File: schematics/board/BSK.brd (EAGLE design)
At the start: 94 x 94 mm, 58 parts

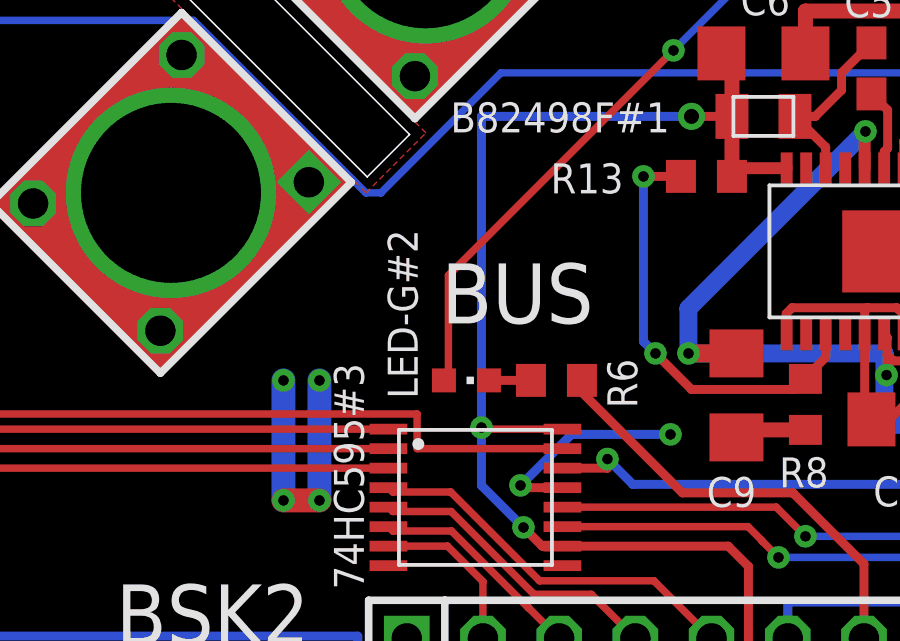
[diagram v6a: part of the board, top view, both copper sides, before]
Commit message: Исправлены RADIO и диоды
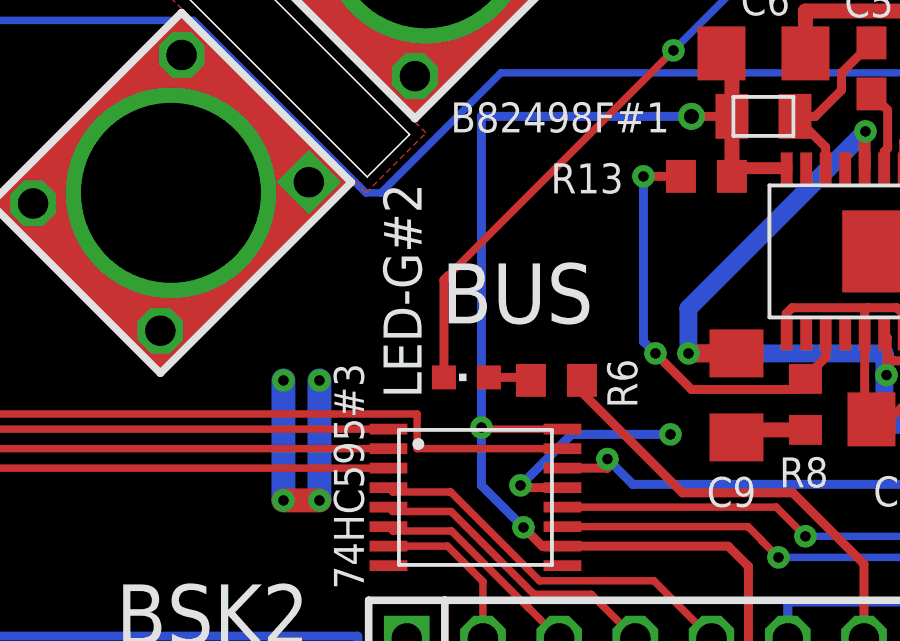
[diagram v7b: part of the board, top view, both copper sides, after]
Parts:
- moved LED-G#2 0.10 mm to (32.1, 16.1), turned to 90 degrees
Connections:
- net BUS-: now also LED-G#2.C; no longer LED-G#2.A
- net N$38: now also LED-G#2.A; no longer LED-G#2.C
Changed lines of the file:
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@@
 <attribute name="VALUE" x="18.405" y="56.53" size="1.27" layer="27" rot="R90"/>
-</element>
-<element name="LED-G#2" library="led" library_urn="urn:adsk.eagle:library:259" package="CHIPLED_0603" package3d_urn="urn:adsk.eagle:package:15822/2" value="" x="32.1" y="16" smashed="yes" rot="R270">
-<attribute name="NAME" x="30.475" y="15.39" size="1" layer="25" rot="R90"/>
-<attribute name="POPULARITY" value="28" x="30.1" y="37" size="1.778" layer="27" rot="R270" display="off"/>
-<attribute name="VALUE" x="30.83" y="14.095" size="1.27" layer="27"/>
 </element>
 <element name="R6" library="resistor" library_urn="urn:adsk.eagle:library:348" package="R0603" package3d_urn="urn:adsk.eagle:package:23555/3" value="2k" x="35.1" y="16" smashed="yes" rot="R180">
@@
 <element name="R14" library="resistor" library_urn="urn:adsk.eagle:library:348" package="R0603" package3d_urn="urn:adsk.eagle:package:23555/3" value="5k1" x="62.1" y="78.7" smashed="yes" rot="R180">
 <attribute name="VALUE" x="62.735" y="80.605" size="1.27" layer="27" rot="R180"/>
+</element>
+<element name="LED-G#2" library="led" library_urn="urn:adsk.eagle:library:259" package="CHIPLED_0603" package3d_urn="urn:adsk.eagle:package:15822/2" value="" x="32.1" y="16.1" smashed="yes" rot="R90">
+<attribute name="NAME" x="29.335" y="22.57" size="1.27" layer="25" rot="R270"/>
+<attribute name="POPULARITY" value="28" x="23.5" y="11.1" size="1.778" layer="27" rot="R90" display="off"/>
+<attribute name="VALUE" x="33.37" y="18.005" size="1.27" layer="27" rot="R180"/>
 </element>
 </elements>
@@
 <contactref element="R20" pad="2"/>
 <contactref element="FS8205A" pad="23"/>
-<contactref element="LED-G#2" pad="A"/>
 <contactref element="U$4" pad="3"/>
 <contactref element="U$4" pad="4"/>
@@
 <wire x1="67.5" y1="63.5" x2="67.85919375" y2="63.616553125" width="0.25" layer="16"/>
 <wire x1="63.5" y1="63.5" x2="63.263" y2="63.263" width="0.25" layer="16"/>
-<wire x1="31.5" y1="19.5" x2="31.5" y2="16" width="0.25" layer="1"/>
 <wire x1="39" y1="27" x2="31.5" y2="19.5" width="0.25" layer="1"/>
 <wire x1="42.75" y1="30.75" x2="39" y2="27" width="0.25" layer="16"/>
@@
 <wire x1="57.19" y1="64.31" x2="55.03" y2="64.31" width="0.25" layer="1"/>
 <wire x1="58.5" y1="63" x2="57.19" y2="64.31" width="0.25" layer="1"/>
-<wire x1="31.5" y1="16" x2="31.35" y2="16" width="0.25" layer="1"/>
 <wire x1="58.5" y1="63" x2="63.263" y2="63.263" width="0.25" layer="1"/>
 <wire x1="58.75" y1="63" x2="58.666803125" y2="62.90944375" width="0.25" layer="1"/>
@@
 <via x="39" y="27" extent="1-16" drill="0.35"/>
 <via x="55.03" y="64.31" extent="1-16" drill="0.35"/>
+<contactref element="LED-G#2" pad="C"/>
+<wire x1="31.5" y1="19.5" x2="31.35" y2="19.35" width="0.3" layer="1"/>
+<wire x1="31.35" y1="19.35" x2="31.35" y2="16.1" width="0.3" layer="1"/>
 </signal>
 <signal name="N$8">
@@
 <wire x1="18.5" y1="58.55" x2="16.5" y2="58.55" width="0.3" layer="1"/>
 </signal>
-<signal name="N$38">
-<contactref element="R6" pad="2"/>
-<contactref element="LED-G#2" pad="C"/>
-<wire x1="32.85" y1="16" x2="34.25" y2="16" width="0.3" layer="1"/>
-</signal>
 <signal name="BUS-1">
 <contactref element="U$2" pad="3"/>
@@
 <wire x1="30.5" y1="63.5" x2="30.737" y2="63.263" width="0.25" layer="1"/>
 </signal>
+<signal name="N$38">
+<contactref element="LED-G#2" pad="A"/>
+<contactref element="R6" pad="2"/>
+<wire x1="32.85" y1="16.1" x2="34.15" y2="16.1" width="0.3" layer="1"/>
+<wire x1="34.15" y1="16.1" x2="34.25" y2="16" width="0.3" layer="1"/>
+</signal>
 </signals>

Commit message: Резисторы у FS8205A 100Ом
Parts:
- R10, R11: value 10k -> 100R
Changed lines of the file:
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@@
 <attribute name="NAME" x="65.456" y="86.078" size="1" layer="25"/>
 </element>
-<element name="R10" library="resistor" library_urn="urn:adsk.eagle:library:348" package="R0603" package3d_urn="urn:adsk.eagle:package:23555/3" value="10k" x="82.8" y="61.7" smashed="yes" rot="R180">
+<element name="R10" library="resistor" library_urn="urn:adsk.eagle:library:348" package="R0603" package3d_urn="urn:adsk.eagle:package:23555/3" value="100R" x="82.8" y="61.7" smashed="yes" rot="R180">
 <attribute name="NAME" x="84.765" y="66.685" size="1" layer="25"/>
 <attribute name="VALUE" x="83.435" y="63.605" size="1.27" layer="27" rot="R180"/>
 </element>
-<element name="R11" library="resistor" library_urn="urn:adsk.eagle:library:348" package="R0603" package3d_urn="urn:adsk.eagle:package:23555/3" value="10k" x="82.8" y="63.9" smashed="yes" rot="R180">
+<element name="R11" library="resistor" library_urn="urn:adsk.eagle:library:348" package="R0603" package3d_urn="urn:adsk.eagle:package:23555/3" value="100R" x="82.8" y="63.9" smashed="yes" rot="R180">
 <attribute name="NAME" x="84.745" y="68.175" size="1" layer="25"/>
 <attribute name="VALUE" x="83.435" y="65.805" size="1.27" layer="27" rot="R180"/>
